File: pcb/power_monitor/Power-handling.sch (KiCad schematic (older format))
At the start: 8 parts, among them K1 G2RL-2A-DC5, Q1 FDN339AN, U2 ACS723xMATR-10AB

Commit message: Fixed power-monitor PCB, to match real-life fixes
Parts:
- C1: footprint Capacitor_SMD:C_0603_1608Metric_Pad0.84x1.00mm_HandSolder -> Capacitor_SMD:C_0603_1608Metric_Pad1.05x0.95mm_HandSolder
- K1: symbol Relay:G2RL-2A -> power_monitor-rescue:G2RL-2A-Relay
- PS1: symbol Power_Management:HLK-PM01 -> power_monitor-rescue:HLK-PM01-Power_Management
- Q1: symbol Device:Q_NMOS_GDS -> Device:Q_NMOS_GSD
- R1: footprint Resistor_SMD:R_0603_1608Metric_Pad0.84x1.00mm_HandSolder -> Resistor_SMD:R_0603_1608Metric_Pad1.05x0.95mm_HandSolder
- U2: symbol Sensor_Current:ACS723xMATR-10AB -> power_monitor-rescue:ACS723xMATR-10AB-Sensor_Current
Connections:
- net GND: now also Q1.2 (S); no longer Q1.3 (S)
- net at D1.2 (A), K1.A1: now also Q1.3 (D); no longer Q1.2 (D)
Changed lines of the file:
@@
 F 0 "R1" H 6309 2371 50  0000 L CNN
 F 1 "15k" H 6309 2280 50  0000 L CNN
-F 2 "Resistor_SMD:R_0603_1608Metric_Pad0.84x1.00mm_HandSolder" H 6250 2325 50  0001 C CNN
+F 2 "Resistor_SMD:R_0603_1608Metric_Pad1.05x0.95mm_HandSolder" H 6250 2325 50  0001 C CNN
 F 3 "~" H 6250 2325 50  0001 C CNN
 	1    6250 2325
@@
 	6000 2200 6000 2150
 $Comp
-L Device:Q_NMOS_GDS Q1
+L Device:Q_NMOS_GSD Q1
 U 1 1 5AC9C39B
 P 6000 2400
@@
 Connection ~ 6250 2150
 $Comp
-L Sensor_Current:ACS723xMATR-10AB U2
+L power_monitor-rescue:ACS723xMATR-10AB-Sensor_Current U2
 U 1 1 5AC9C3A9
 P 6550 3850
@@
 F 0 "C1" H 7683 4104 50  0000 R CNN
 F 1 "0.1uF" H 7683 4195 50  0000 R CNN
-F 2 "Capacitor_SMD:C_0603_1608Metric_Pad0.84x1.00mm_HandSolder" H 7775 4150 50  0001 C CNN
+F 2 "Capacitor_SMD:C_0603_1608Metric_Pad1.05x0.95mm_HandSolder" H 7775 4150 50  0001 C CNN
 F 3 "~" H 7775 4150 50  0001 C CNN
 	1    7775 4150
@@
 	5725 3250 5650 3250
 $Comp
-L Relay:G2RL-2A K1
+L power_monitor-rescue:G2RL-2A-Relay K1
 U 1 1 5AC87461
 P 5350 3150
@@
 $EndComp
 $Comp
-L Power_Management:HLK-PM01 PS1
+L power_monitor-rescue:HLK-PM01-Power_Management PS1
 U 1 1 5AC93002
 P 6425 5000

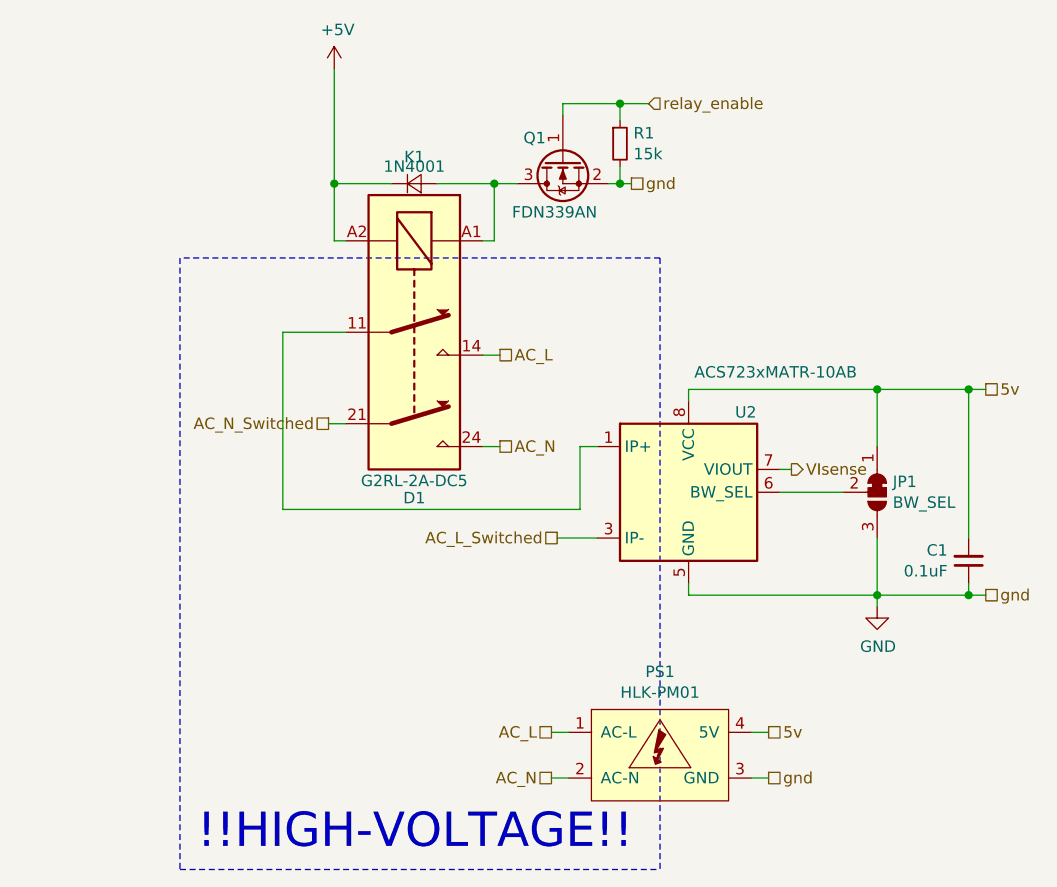
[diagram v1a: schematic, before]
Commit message: Updated power_monitor pcb to use IRM-02 PSU
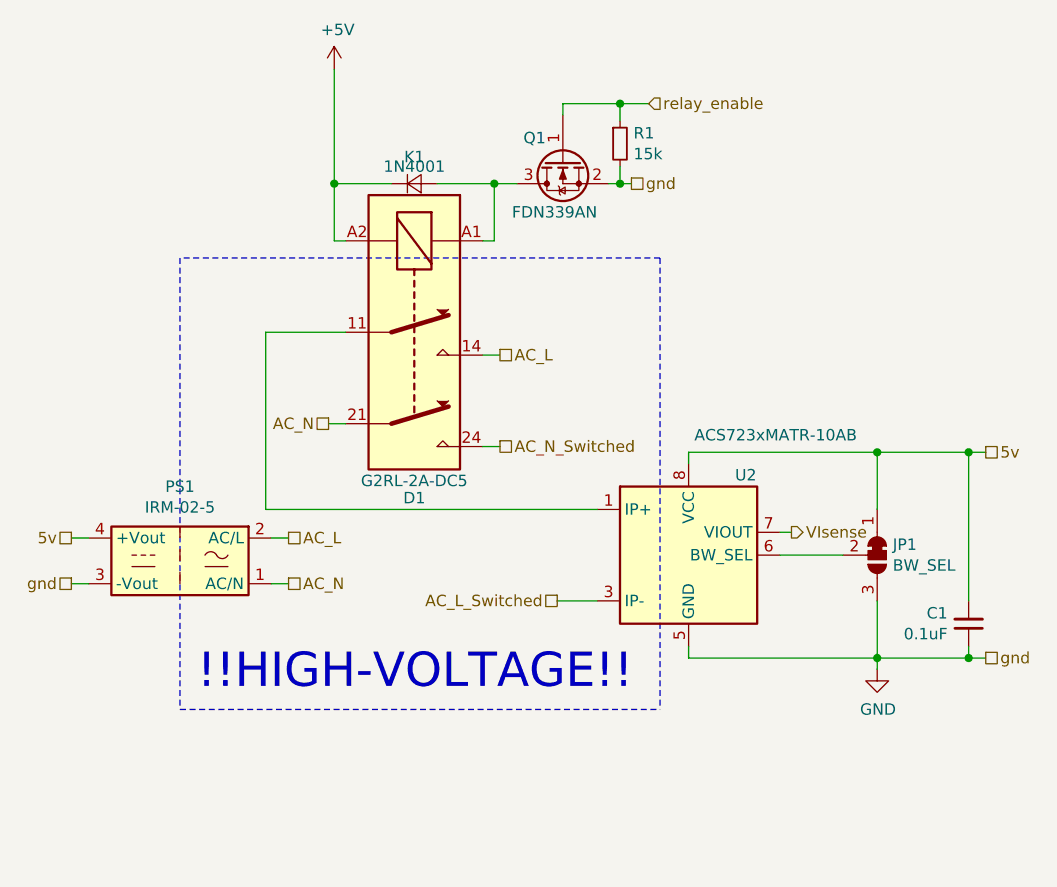
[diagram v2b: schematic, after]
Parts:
- removed PS1: HLK-PM01, Converter_ACDC:HLK-PM01, symbol power_monitor-rescue:HLK-PM01-Power_Management
- added PS1: IRM-02-5, Converter_ACDC:Converter_ACDC_MeanWell_IRM-02-xx_THT, symbol Converter_ACDC:IRM-02-5
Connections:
- net 5v: now also PS1.4 (+Vout)
- net AC_L: now also PS1.2 (AC/L)
- net AC_N: now also K1.21, PS1.1 (AC/N); no longer K1.24
- net AC_N_Switched: now also K1.24; no longer K1.21
- net GND: now also PS1.3 (-Vout)
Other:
- moved on the sheet: C1, JP1, U2
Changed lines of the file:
@@
 L power:GND #PWR0103
 U 1 1 5AC9C331
-P 7375 4350
-F 0 "#PWR0103" H 7375 4100 50  0001 C CNN
-F 1 "GND" H 7300 4175 50  0000 L CNN
-F 2 "" H 7375 4350 50  0001 C CNN
-F 3 "" H 7375 4350 50  0001 C CNN
-	1    7375 4350
-	1    0    0    -1
-$EndComp
-Wire Wire Line
-	6550 4250 6550 4300
+P 7375 4625
+F 0 "#PWR0103" H 7375 4375 50  0001 C CNN
+F 1 "GND" H 7300 4450 50  0000 L CNN
+F 2 "" H 7375 4625 50  0001 C CNN
+F 3 "" H 7375 4625 50  0001 C CNN
+	1    7375 4625
+	1    0    0    -1
+$EndComp
+Wire Wire Line
+	6550 4525 6550 4575
 Wire Wire Line
 	5725 3650 5650 3650
 Wire Wire Line
-	6150 4050 5975 4050
+	6150 4325 5975 4325
 $Comp
 L Device:D_Small D1
@@
 L power_monitor-rescue:ACS723xMATR-10AB-Sensor_Current U2
 U 1 1 5AC9C3A9
-P 6550 3850
-F 0 "U2" H 6800 4200 50  0000 C CNN
-F 1 "ACS723xMATR-10AB" H 6575 4375 50  0000 L CNN
-F 2 "Package_SO:SOIC-8_3.9x4.9mm_P1.27mm" H 6900 3800 50  0001 L CIN
-F 3 "http://www.allegromicro.com/~/media/Files/Datasheets/ACS723KMA-Datasheet.ashx?la=en" H 6550 3850 50  0001 C CNN
-	1    6550 3850
+P 6550 4125
+F 0 "U2" H 6800 4475 50  0000 C CNN
+F 1 "ACS723xMATR-10AB" H 6575 4650 50  0000 L CNN
+F 2 "Package_SO:SOIC-8_3.9x4.9mm_P1.27mm" H 6900 4075 50  0001 L CIN
+F 3 "http://www.allegromicro.com/~/media/Files/Datasheets/ACS723KMA-Datasheet.ashx?la=en" H 6550 4125 50  0001 C CNN
+	1    6550 4125
 	1    0    0    -1
 $EndComp
@@
 L Jumper:SolderJumper_3_Bridged12 JP1
 U 1 1 5AC9C3B0
-P 7375 3850
-F 0 "JP1" V 7329 3918 50  0000 L CNN
-F 1 "BW_SEL" V 7420 3918 50  0000 L CNN
-F 2 "Jumper:SolderJumper-3_P1.3mm_Bridged2Bar12_RoundedPad1.0x1.5mm_NumberLabels" H 7375 3850 50  0001 C CNN
-F 3 "~" H 7375 3850 50  0001 C CNN
-	1    7375 3850
+P 7375 4125
+F 0 "JP1" V 7329 4193 50  0000 L CNN
+F 1 "BW_SEL" V 7420 4193 50  0000 L CNN
+F 2 "Jumper:SolderJumper-3_P1.3mm_Bridged2Bar12_RoundedPad1.0x1.5mm_NumberLabels" H 7375 4125 50  0001 C CNN
+F 3 "~" H 7375 4125 50  0001 C CNN
+	1    7375 4125
 	0    1    1    0
 $EndComp
 Wire Wire Line
-	6550 3400 7375 3400
-Wire Wire Line
-	7375 3400 7375 3650
-Wire Wire Line
-	6550 3400 6550 3450
-Wire Wire Line
-	7375 4300 7375 4050
-Wire Wire Line
-	6950 3750 7000 3750
+	6550 3675 7375 3675
+Wire Wire Line
+	7375 3675 7375 3925
+Wire Wire Line
+	6550 3675 6550 3725
+Wire Wire Line
+	7375 4575 7375 4325
+Wire Wire Line
+	6950 4025 7000 4025
 $Comp
 L Device:C_Small C1
 U 1 1 5AC9C3C1
-P 7775 4150
-F 0 "C1" H 7683 4104 50  0000 R CNN
-F 1 "0.1uF" H 7683 4195 50  0000 R CNN
-F 2 "Capacitor_SMD:C_0603_1608Metric_Pad1.05x0.95mm_HandSolder" H 7775 4150 50  0001 C CNN
-F 3 "~" H 7775 4150 50  0001 C CNN
-	1    7775 4150
+P 7775 4425
+F 0 "C1" H 7683 4379 50  0000 R CNN
+F 1 "0.1uF" H 7683 4470 50  0000 R CNN
+F 2 "Capacitor_SMD:C_0603_1608Metric_Pad1.05x0.95mm_HandSolder" H 7775 4425 50  0001 C CNN
+F 3 "~" H 7775 4425 50  0001 C CNN
+	1    7775 4425
 	1    0    0    1
 $EndComp
 Wire Wire Line
-	7375 4300 7775 4300
-Wire Wire Line
-	7775 4300 7775 4250
-Connection ~ 7375 4300
-Wire Wire Line
-	7775 4050 7775 3400
-Wire Wire Line
-	7775 3400 7375 3400
-Connection ~ 7375 3400
+	7375 4575 7775 4575
+Wire Wire Line
+	7775 4575 7775 4525
+Connection ~ 7375 4575
+Wire Wire Line
+	7775 4325 7775 3675
+Wire Wire Line
+	7775 3675 7375 3675
+Connection ~ 7375 3675
 Wire Notes Line
 	6425 2825 4325 2825
 Wire Notes Line
-	4325 2825 4325 5500
-Wire Notes Line
-	4325 5500 6425 5500
-Wire Notes Line
-	6425 2825 6425 5500
-Text Notes 4400 5425 0    150  ~ 0
+	4325 2825 4325 4800
+Wire Notes Line
+	4325 4800 6425 4800
+Wire Notes Line
+	6425 2825 6425 4800
+Text Notes 4400 4725 0    150  ~ 0
 !!HIGH-VOLTAGE!!
-Text HLabel 7000 3750 2    50   Output ~ 0
+Text HLabel 7000 4025 2    50   Output ~ 0
 VIsense
 Text HLabel 6375 2150 2    50   Input ~ 0
 relay_enable
+Text HLabel 5725 3650 2    50   UnSpc ~ 0
+AC_N_Switched
+Text HLabel 5975 4325 0    50   UnSpc ~ 0
+AC_L_Switched
 Text HLabel 4975 3550 0    50   UnSpc ~ 0
-AC_N_Switched
-Text HLabel 5975 4050 0    50   UnSpc ~ 0
-AC_L_Switched
-Text HLabel 5725 3650 2    50   UnSpc ~ 0
 AC_N
 Text HLabel 5725 3250 2    50   UnSpc ~ 0
@@
 	-1   0    0    1
 $EndComp
-$Comp
-L power_monitor-rescue:HLK-PM01-Power_Management PS1
-U 1 1 5AC93002
-P 6425 5000
-F 0 "PS1" H 6425 5365 50  0000 C CNN
-F 1 "HLK-PM01" H 6425 5274 50  0000 C CNN
-F 2 "Converter_ACDC:HLK-PM01" H 5275 4650 50  0001 C CNN
-F 3 "" H 5275 4650 50  0001 C CNN
-	1    6425 5000
-	1    0    0    -1
-$EndComp
-Wire Wire Line
-	7375 4300 7375 4350
-Wire Wire Line
-	6825 5100 6900 5100
-Wire Wire Line
-	5950 5100 6025 5100
-Text HLabel 5950 5100 0    50   UnSpc ~ 0
+Wire Wire Line
+	7375 4575 7375 4625
+Wire Wire Line
+	3925 4250 3850 4250
+Wire Wire Line
+	4800 4250 4725 4250
+Text HLabel 4800 4250 2    50   UnSpc ~ 0
 AC_N
-Text HLabel 5950 4900 0    50   UnSpc ~ 0
+Text HLabel 4800 4050 2    50   UnSpc ~ 0
 AC_L
 Wire Wire Line
-	5950 4900 6025 4900
-Wire Wire Line
-	6950 3850 7225 3850
-Wire Wire Line
-	6550 4300 7375 4300
-Wire Wire Line
-	4975 3550 5050 3550
-Wire Wire Line
-	6150 3650 6075 3650
-Wire Wire Line
-	6075 3925 4775 3925
-Wire Wire Line
-	4775 3150 5050 3150
-Wire Wire Line
-	6075 3650 6075 3925
-Wire Wire Line
-	4775 3150 4775 3925
-Text HLabel 7850 3400 2    50   UnSpc ~ 0
+	4800 4050 4725 4050
+Wire Wire Line
+	6950 4125 7225 4125
+Wire Wire Line
+	6550 4575 7375 4575
+Text HLabel 7850 3675 2    50   UnSpc ~ 0
 5v
 Wire Wire Line
-	7775 3400 7850 3400
-Connection ~ 7775 3400
-Text HLabel 6900 4900 2    50   UnSpc ~ 0
+	7775 3675 7850 3675
+Connection ~ 7775 3675
+Text HLabel 3850 4050 0    50   UnSpc ~ 0
 5v
 Wire Wire Line
-	6825 4900 6900 4900
-Text HLabel 7850 4300 2    50   UnSpc ~ 0
+	3925 4050 3850 4050
+Text HLabel 7850 4575 2    50   UnSpc ~ 0
 gnd
 Wire Wire Line
-	7775 4300 7850 4300
-Connection ~ 7775 4300
+	7775 4575 7850 4575
+Connection ~ 7775 4575
 Text HLabel 6300 2500 2    50   UnSpc ~ 0
 gnd
@@
 	6250 2500 6300 2500
 Connection ~ 6250 2500
-Text HLabel 6900 5100 2    50   UnSpc ~ 0
+Text HLabel 3850 4250 0    50   UnSpc ~ 0
 gnd
 Wire Wire Line
 	5000 2000 5000 2500
+$Comp
+L Converter_ACDC:IRM-02-5 PS1
+U 1 1 5C831918
+P 4325 4150
+F 0 "PS1" H 4325 4475 50  0000 C CNN
+F 1 "IRM-02-5" H 4325 4384 50  0000 C CNN
+F 2 "Converter_ACDC:Converter_ACDC_MeanWell_IRM-02-xx_THT" H 4325 3850 50  0001 C CNN
+F 3 "http://www.meanwell.com/productPdf.aspx?i=675" H 4725 3800 50  0001 C CNN
+	1    4325 4150
+	-1   0    0    -1
+$EndComp
+Wire Wire Line
+	4975 3550 5050 3550
+Wire Wire Line
+	4700 3925 4700 3150
+Wire Wire Line
+	4700 3150 5050 3150
+Wire Wire Line
+	4700 3925 6150 3925
 $EndSCHEMATC
